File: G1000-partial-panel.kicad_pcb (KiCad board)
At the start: 2 copper layers, 100 x 100 mm, 3 parts

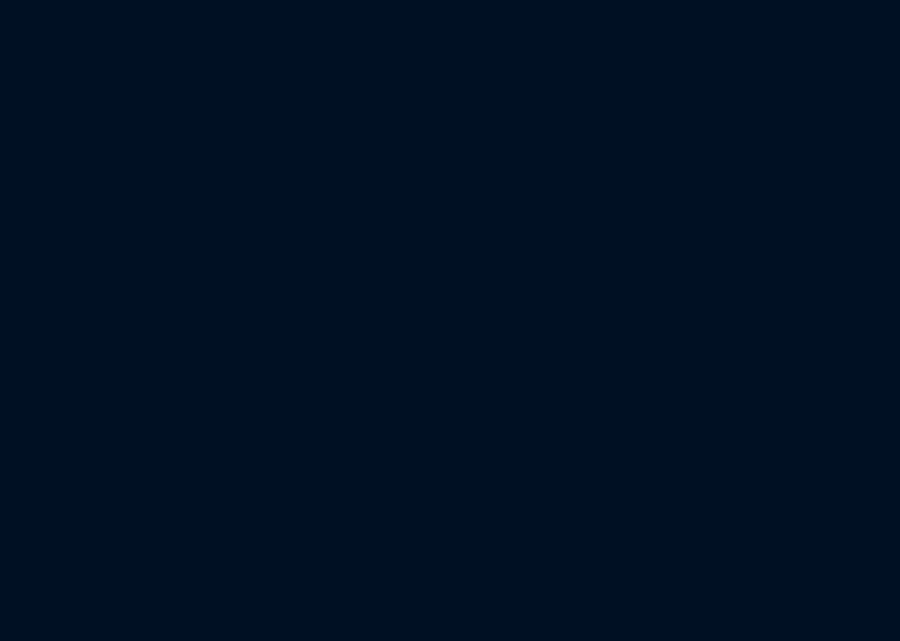
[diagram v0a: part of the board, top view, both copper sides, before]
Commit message: Redo panel
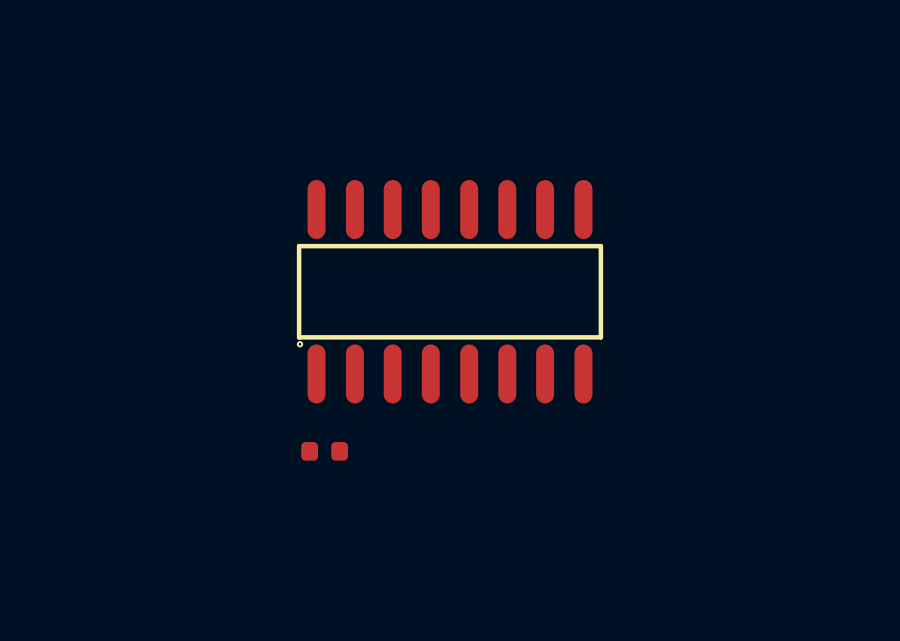
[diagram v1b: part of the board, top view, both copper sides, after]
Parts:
- added R1: 10kΩ, PCM_JLCPCB:R_0402, F.Cu at (65.4, 77.6)
- added U1: 74HC595D, PCM_JLCPCB:SOIC-16_L9.9-W3.9-P1.27-LS6.0-BL, F.Cu at (69.5, 72.3)
